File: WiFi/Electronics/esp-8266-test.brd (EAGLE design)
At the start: 95.2 x 43.2 mm, 16 parts, among them IC2 7805DT, Q1 FDD8870, X1 MKDSN1,5/2-5,08, X2 MKDSN1,5/2-5,08

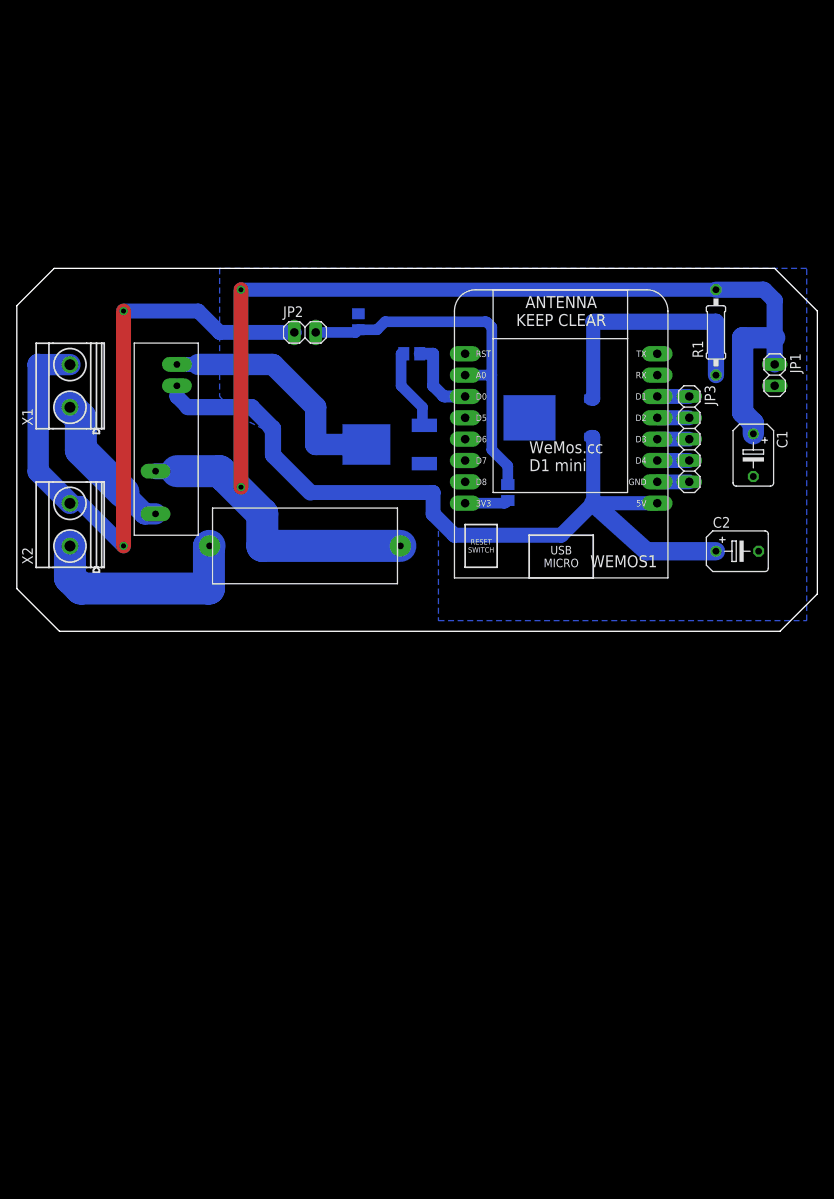
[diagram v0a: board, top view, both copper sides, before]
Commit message: heating.php improved to check that times monotonically increase throughout the day.
Various bits of experimental WiFi electronics added.
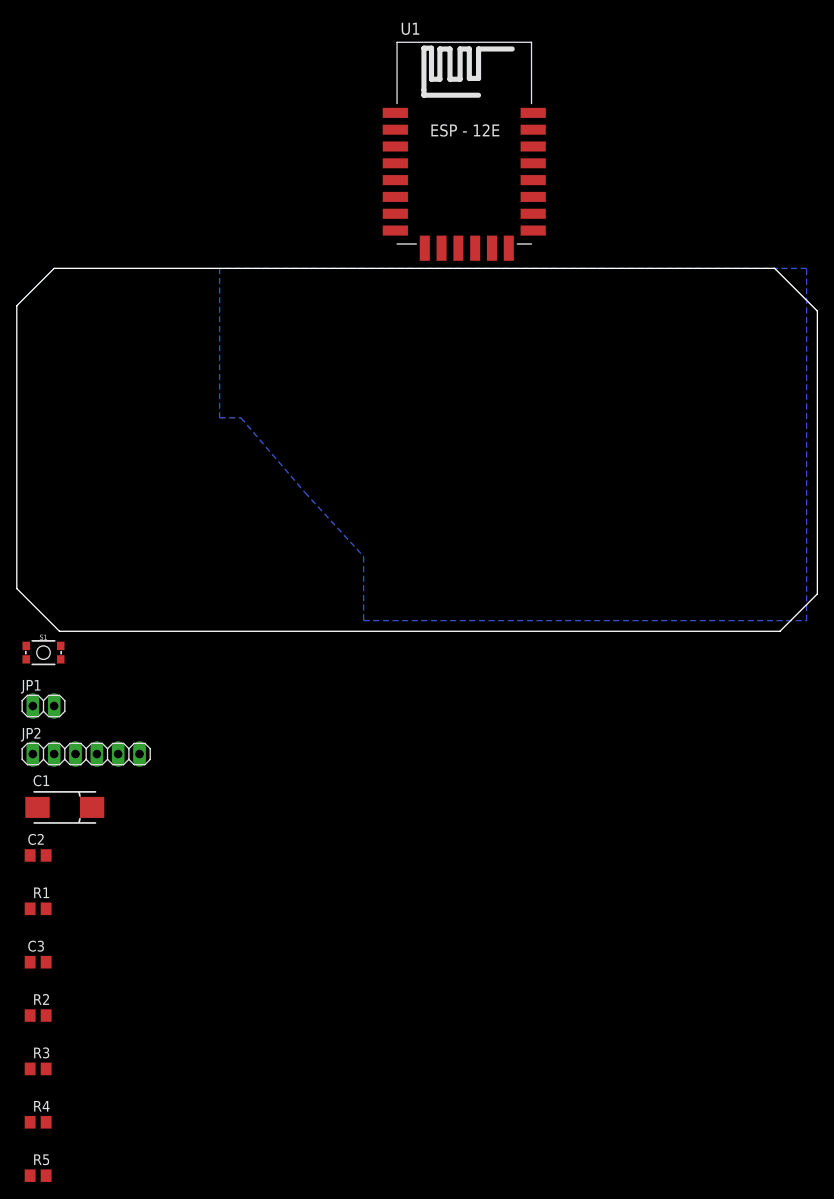
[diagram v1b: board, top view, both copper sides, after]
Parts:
- removed IC2: 7805DT, adafruit:TO252
- removed JP3: (no value), pinhead:1X05
- removed Q1: FDD8870, SparkFun-DiscreteSemi:DPAK
- removed U$1: OMRON-G6DS, alexa:OMRON-G6DS-1A-H
- removed U$2: FUSE, alexa:FUSE
- removed WEMOS1: (no value), esp8266modules:WEMOS-D1-MINI
- removed X1, X2: MKDSN1,5/2-5,08, con-phoenix-508:MKDSN1,5/2-5,08
- added R4, R5: 10K, rcl:R0805
- added S1: (no value), SparkFun-Switches:TACTILE_SWITCH_SMD_4.6X2.8MM
- added U1: (no value), esp8266modules:ESP12E-SMD
- C1: value 1000uF -> 100u; device rcl:B45181B -> rcl:085CS_1AR
- C2: value 1000uF -> 0.1u; device rcl:B45181B -> rcl:C0805
- C3: value 1uF -> 0.1u
- JP2: device pinhead:1X02 -> pinhead:1X06
- R1: value 27R -> 10K; device rcl:0207/10 -> rcl:R0805
- R2: value 1K -> 10K; device rcl:M0805 -> rcl:R0805
- R3: device rcl:M0805 -> rcl:R0805
- moved R1 105.9 mm to (2.54, -34.3), turned to 0 degrees
- moved R3 96.0 mm to (2.54, -53.3), flipped to the top, turned to 0 degrees
- moved JP1 95.5 mm to (3.17, -10.2), turned to 0 degrees
- moved C1 92.0 mm to (5.71, -22.2), turned to 0 degrees
- moved C2 90.7 mm to (2.54, -27.9)
- moved C3 85.2 mm to (2.54, -40.6), flipped to the top, turned to 0 degrees
- moved R2 83.6 mm to (2.54, -47.0), flipped to the top, turned to 0 degrees
- moved JP2 56.5 mm to (8.26, -15.9)
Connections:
- removed net +12V: C1.+, JP1.1, R1.2, U$1.P$3, U$2.P$1
- removed net +5V: C2.+, IC2.2, U$1.P$2, WEMOS1.5V
- removed net N$10: U$1.P$4, X1.1
- removed net N$11: JP3.4, WEMOS1.D4
- removed net N$12: U$2.P$2, X2.1
- removed net N$13: JP3.3, WEMOS1.D3
- removed net N$14: JP3.2, WEMOS1.D2
- removed net N$15: JP3.1, WEMOS1.D1
- new net +3V3: C1.+, C2.1, R1.2, R2.2, R4.2, R5.2, U1.VCC
- new net N$1: C3.1, R1.1, S1.1, S1.2, U1.RESET
- net GND: now also C2.2, R3.1, S1.3, S1.4, U1.GND; no longer C2.-, IC2.3, JP3.5, Q1.3, WEMOS1.GND, X1.2, X2.2
- net N$2: now also JP1.1, R2.1, U1.GPIO0; no longer IC2.1, R1.1
- net N$3: now also JP2.4, U1.RXD0; no longer C3.1, JP2.2, R2.2, WEMOS1.A0
- net N$4: now also R3.2, U1.GPIO15; no longer R2.1, WEMOS1.3V3
- net N$5: now also JP2.5, U1.TXD0; no longer Q1.1, R3.1
- net N$6: now also R4.1, U1.CH_PD; no longer R3.2, WEMOS1.D0
- net N$7: now also R5.1, U1.GPIO2; no longer Q1.4, U$1.P$1
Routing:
- net +12V: track 148.4 -> 0.00 mm, vias 2 -> 0
- net +5V: track 95.1 -> 0.00 mm
- net GND: track 83.5 -> 0.00 mm, vias 2 -> 0
- net N$3: track 44.4 -> 0.00 mm
- net N$2: track 30.4 -> 0.00 mm
- net N$7: track 29.1 -> 0.00 mm
- net N$12: track 25.9 -> 0.00 mm
- net N$10: track 17.6 -> 0.00 mm
- net N$5: track 9.98 -> 0.00 mm
- net N$6: track 9.72 -> 0.00 mm
- net N$4: track 5.20 -> 0.00 mm
- net N$15: track 3.81 -> 0.00 mm
- net N$14: track 3.81 -> 0.00 mm
- net N$13: track 3.81 -> 0.00 mm
- net N$11: track 3.81 -> 0.00 mm
